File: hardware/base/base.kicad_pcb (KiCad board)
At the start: 4 copper layers, 60 x 40 mm, 70 parts, among them J1 Debug, J2 USB_B_Mini, J3 Serial Interface, J4 SWD, J5 OLED Display, J6 Conn_01x02_Pin, M1 Fan_ALT, Q1 Q_NMOS_GSD, Q2 Q_NMOS_GSD, Q3 Q_NMOS_GSD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

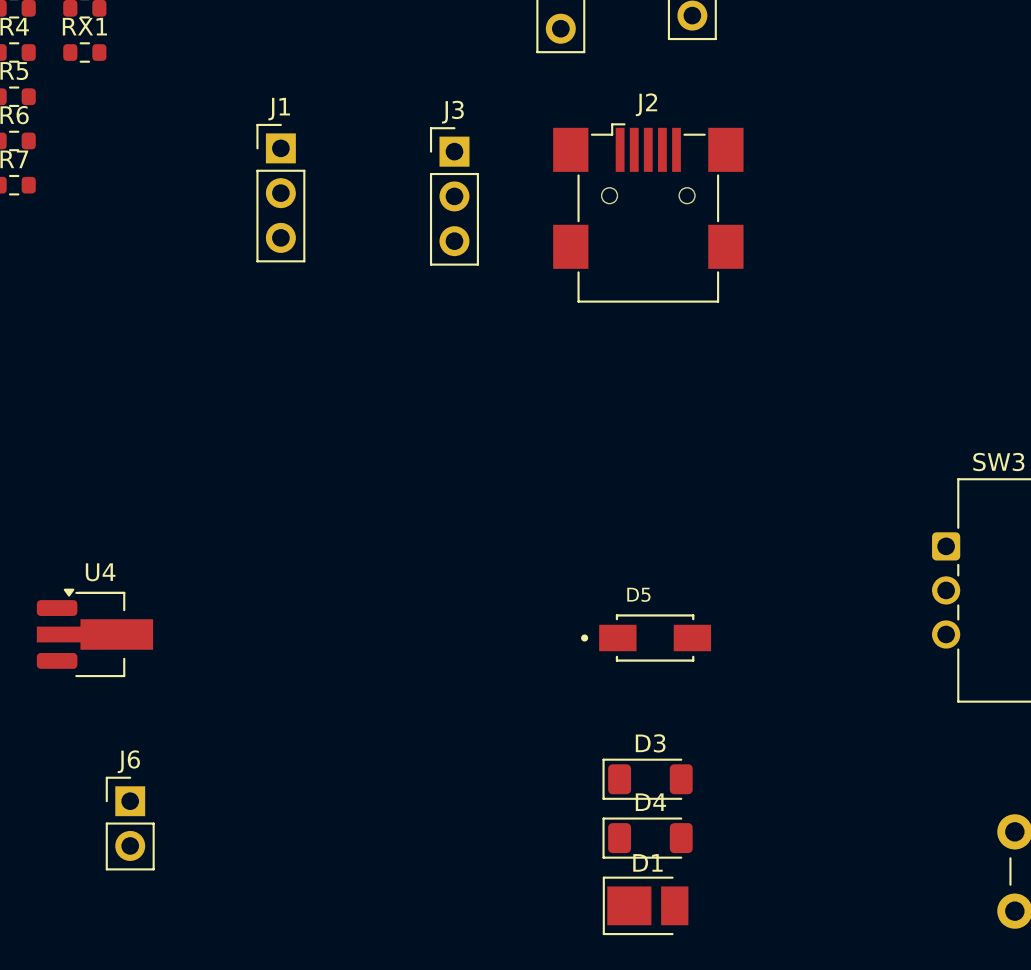
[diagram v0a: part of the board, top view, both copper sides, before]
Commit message: Update PCB and Schema after symbol change
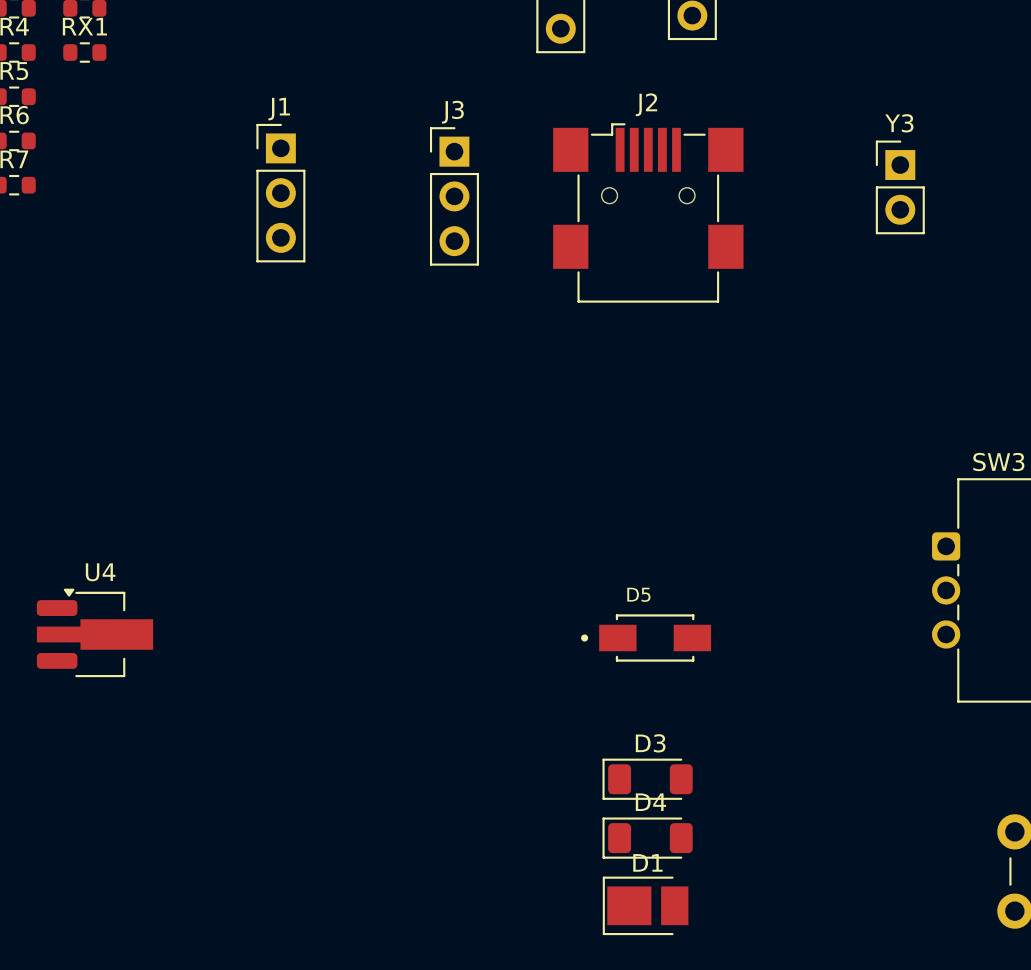
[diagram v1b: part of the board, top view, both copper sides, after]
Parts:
- removed J6: Conn_01x02_Pin, Connector_PinHeader_2.54mm:PinHeader_1x02_P2.54mm_Vertical
- added Y3: 1.70 MHz, Connector_PinHeader_2.54mm:PinHeader_1x02_P2.54mm_Vertical, F.Cu at (91.4, 60.9)

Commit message: did some layout and routing
CHANGELOG
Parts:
- moved C4 144.3 mm to (173.0, 62.7), turned to 180 degrees
- moved C3 143.8 mm to (172.7, 55.4), turned to 180 degrees
- moved C6 141.0 mm to (169.9, 62.7), turned to 180 degrees
- moved C5 140.3 mm to (169.2, 61.2)
- moved C15 138.6 mm to (170.9, 44.8)
- moved C7 136.9 mm to (166.0, 64.0), turned to 180 degrees
- moved C2 136.6 mm to (165.2, 58.4), turned to 90 degrees
- moved C8 136.1 mm to (165.2, 65.6)
- moved C21 132.0 mm to (168.6, 43.2), turned to -90 degrees
- moved C1 130.4 mm to (158.9, 56.8), turned to 90 degrees
- moved L1 129.8 mm to (170.9, 46.4), turned to 180 degrees
- moved R1 128.2 mm to (168.9, 57.1), turned to 90 degrees
- moved R4 127.5 mm to (167.9, 40.9)
- moved C9 126.8 mm to (158.1, 65.6), turned to 180 degrees
- moved R11 125.9 mm to (171.0, 48.0)
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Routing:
- net Net-(J5-Pin_4): track 0.00 -> 42.0 mm, vias 0 -> 1
- net Net-(J5-Pin_3): track 0.00 -> 41.3 mm, vias 0 -> 1
- net Net-(J4-Pin_3): track 0.00 -> 33.1 mm, vias 0 -> 2
- net Net-(J4-Pin_1): track 0.00 -> 32.3 mm, vias 0 -> 2
- net Net-(J4-Pin_2): track 0.00 -> 30.0 mm, vias 0 -> 2
- net Net-(J3-Pin_1): track 0.00 -> 26.4 mm, vias 0 -> 2
- net /VBUS: track 0.00 -> 25.7 mm, vias 0 -> 4
- net Net-(U3-OUTN): track 0.00 -> 25.4 mm
- net Net-(U3-OUTP): track 0.00 -> 24.6 mm
- net Net-(J3-Pin_2): track 0.00 -> 24.5 mm, vias 0 -> 2
- net Net-(U1-P0.01/XL2): track 0.00 -> 24.0 mm, vias 0 -> 1
- net /DETECT_VSOURCE: track 0.00 -> 24.0 mm, vias 0 -> 2
- net Net-(BT1-+): track 0.00 -> 20.9 mm, vias 0 -> 2
- net Net-(U1-P0.00/XL1): track 0.00 -> 20.4 mm, vias 0 -> 1
- net Net-(J2-D-): track 0.00 -> 20.3 mm, vias 0 -> 2
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- added copper zone on In1.Cu, net +3.3V
- added copper zone on B.Cu, net /VBUS
- added copper zone on F.Cu, net GND
- added copper zone on In2.Cu, net GND

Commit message: Changelog
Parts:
- moved SW3 3.51 mm to (117.5, 94.0)
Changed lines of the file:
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@@
 		)
 		(fp_text user "${REFERENCE}"
-			(at 0 1.270001 360)
+			(at 0 1.270001 0)
 			(layer "F.Fab")
 			(effects
@@
 		(tags "inductor")
 		(property "Reference" "L1"
-			(at 0 -1.43 360)
+			(at 0 -1.43 0)
 			(layer "F.SilkS")
 			(effects
@@
 		)
 		(property "Value" "300 uH"
-			(at 0 1.43 360)
+			(at 0 1.43 0)
 			(layer "F.Fab")
 			(effects
@@
 		)
 		(fp_text user "${REFERENCE}"
-			(at 0 0 360)
+			(at 0 0 0)
 			(layer "F.Fab")
 			(effects
@@
 		(tags "TQFN NoLead")
 		(property "Reference" "U3"
-			(at 0 -2.8 360)
+			(at 0 -2.8 0)
 			(layer "F.SilkS")
 			(effects
@@
 		)
 		(property "Value" "MAX98357A"
-			(at 0 2.8 360)
+			(at 0 2.8 0)
 			(layer "F.Fab")
 			(effects
@@
 		)
 		(fp_text user "${REFERENCE}"
-			(at 0 0 360)
+			(at 0 0 0)
 			(layer "F.Fab")
 			(effects
@@
 		(tags "capacitor")
 		(property "Reference" "C4"
-			(at 0 -1.43 360)
+			(at 0 -1.43 0)
 			(layer "F.SilkS")
 			(effects
@@
 		)
 		(property "Value" "12pF"
-			(at 0 1.43 360)
+			(at 0 1.43 0)
 			(layer "F.Fab")
 			(effects
@@
 		)
 		(fp_text user "${REFERENCE}"
-			(at 0 0 360)
+			(at 0 0 0)
 			(layer "F.Fab")
 			(effects
@@
 		(tags "capacitor")
 		(property "Reference" "C3"
-			(at 0 -1.43 360)
+			(at 0 -1.43 0)
 			(layer "F.SilkS")
 			(effects
@@
 		)
 		(property "Value" "12pF"
-			(at 0 1.43 360)
+			(at 0 1.43 0)
 			(layer "F.Fab")
 			(effects
@@
 		)
 		(fp_text user "${REFERENCE}"
-			(at 0 0 360)
+			(at 0 0 0)
 			(layer "F.Fab")
 			(effects
@@
 		(tags "QFN NoLead")
 		(property "Reference" "U1"
-			(at 0 -3.8 360)
+			(at 0 -3.8 0)
 			(layer "F.SilkS")
 			(effects
@@
 		)
 		(property "Value" "nRF52833-QDxx"
-			(at 0 3.8 360)
+			(at 0 3.8 0)
 			(layer "F.Fab")
 			(effects
@@
 		)
 		(fp_text user "${REFERENCE}"
-			(at 0 0 360)
+			(at 0 0 0)
 			(layer "F.Fab")
 			(effects
@@
 		(tags "capacitor")
 		(property "Reference" "C8"
-			(at 0 -1.43 360)
+			(at 0 -1.43 0)
 			(layer "F.SilkS")
 			(effects
@@
 		)
 		(property "Value" "100nf"
-			(at 0 1.43 360)
+			(at 0 1.43 0)
 			(layer "F.Fab")
 			(effects
@@
 		)
 		(fp_text user "${REFERENCE}"
-			(at 0 0 360)
+			(at 0 0 0)
 			(layer "F.Fab")
 			(effects
@@
 		)
 		(fp_text user "${REFERENCE}"
-			(at 0 1.270001 360)
+			(at 0 1.270001 0)
 			(layer "F.Fab")
 			(effects
@@
 		)
 		(fp_text user "${REFERENCE}"
-			(at 0 1 360)
+			(at 0 1 0)
 			(layer "F.Fab")
 			(effects
@@
 		(tags "['AT310']")
 		(property "Reference" "Y1"
-			(at -1.75 3 360)
+			(at -1.75 3 0)
 			(layer "F.SilkS")
 			(effects
@@
 		)
 		(property "Value" "32kHz"
-			(at 4.29 3 360)
+			(at 4.29 3 0)
 			(layer "F.Fab")
 			(effects
@@
 		)
 		(fp_text user "${REFERENCE}"
-			(at 1.25 8.75 360)
+			(at 1.25 8.75 0)
 			(layer "F.Fab")
 			(effects
@@
 		)
 		(fp_text user "${REFERENCE}"
-			(at 0.199999 0 360)
+			(at 0.199999 0 0)
 			(layer "F.Fab")
 			(effects
@@
 		(tags "capacitor")
 		(property "Reference" "C23"
-			(at 0 -1.43 360)
+			(at 0 -1.43 0)
 			(layer "F.SilkS")
 			(effects
@@
 		)
 		(property "Value" "0.1 uF"
-			(at 0 1.43 360)
+			(at 0 1.43 0)
 			(layer "F.Fab")
 			(effects
@@
 		)
 		(fp_text user "${REFERENCE}"
-			(at 0 0 360)
+			(at 0 0 0)
 			(layer "F.Fab")
 			(effects
@@
 		(tags "capacitor")
 		(property "Reference" "C11"
-			(at 0 -1.43 360)
+			(at 0 -1.43 0)
 			(layer "F.SilkS")
 			(effects
@@
 		)
 		(property "Value" "4.7uF"
-			(at 0 1.43 360)
+			(at 0 1.43 0)
 			(layer "F.Fab")
 			(effects
@@
 		)
 		(fp_text user "${REFERENCE}"
-			(at 0 0 360)
+			(at 0 0 0)
 			(layer "F.Fab")
 			(effects
@@
 		(tags "Through hole pin header THT 1x03 2.54mm single row")
 		(property "Reference" "J3"
-			(at 0 -2.33 360)
+			(at 0 -2.33 0)
 			(layer "F.SilkS")
 			(effects
@@
 		)
 		(property "Value" "Serial Interface"
-			(at 0 7.41 360)
+			(at 0 7.41 0)
 			(layer "F.Fab")
 			(effects
@@
 		(tags "SOT TO_SOT_SMD")
 		(property "Reference" "Q4"
-			(at 0 -2.4 360)
+			(at 0 -2.4 0)
 			(layer "F.SilkS")
 			(effects
@@
 		)
 		(property "Value" "MMBT2222A"
-			(at 0 2.4 360)
+			(at 0 2.4 0)
 			(layer "F.Fab")
 			(effects
@@
 		)
 		(fp_text user "${REFERENCE}"
-			(at 0 0 360)
+			(at 0 0 0)
 			(layer "F.Fab")
 			(effects
@@
 	(footprint "Rotary_Encoder:RotaryEncoder_Bourns_Vertical_PEC12R-3x17F-Sxxxx"
 		(layer "F.Cu")
-		(at 117.75 97.5)
+		(at 117.5 94)
 		(descr "Bourns rotary encoder, PEC12R, with switch, with bushing, vertical shaft, 17.5mm shaft, https://www.bourns.com/docs/product-datasheets/pec12r.pdf")
 		(tags "rotary encoder")
@@
 		(tags "test point THT pad rectangle square")
 		(property "Reference" "TP1"
-			(at 0 -1.648 360)
+			(at 0 -1.648 0)
 			(layer "F.SilkS")
 			(effects
@@
 		)
 		(property "Value" "TestPoint"
-			(at 0 1.75 360)
+			(at 0 1.75 0)
 			(layer "F.Fab")
 			(effects
@@
 		)
 		(fp_text user "${REFERENCE}"
-			(at 0 -1.65 360)
+			(at 0 -1.65 0)
 			(layer "F.Fab")
 			(effects
@@
 		(tags "SOT TO_SOT_SMD")
 		(property "Reference" "Q2"
-			(at 0 -2.4 360)
+			(at 0 -2.4 0)
 			(layer "F.SilkS")
 			(effects
@@
 		)
 		(property "Value" "Q_NMOS_GSD"
-			(at 0 2.4 360)
+			(at 0 2.4 0)
 			(layer "F.Fab")
 			(effects
@@
 		)
 		(fp_text user "${REFERENCE}"
-			(at 0 0 360)
+			(at 0 0 0)
 			(layer "F.Fab")
 			(effects
@@
 		(tags "capacitor")
 		(property "Reference" "C16"
-			(at 0 -1.43 360)
+			(at 0 -1.43 0)
 			(layer "F.SilkS")
 			(effects
@@
 		)
 		(property "Value" "1uF"
-			(at 0 1.43 360)
+			(at 0 1.43 0)
 			(layer "F.Fab")
 			(effects
@@
 		)
 		(fp_text user "${REFERENCE}"
-			(at 0 0 360)
+			(at 0 0 0)
 			(layer "F.Fab")
 			(effects
@@
 		(tags "capacitor")
 		(property "Reference" "C10"
-			(at 0 -1.43 360)
+			(at 0 -1.43 0)
 			(layer "F.SilkS")
 			(effects
@@
 		)
 		(property "Value" "4.7uF"
-			(at 0 1.43 360)
+			(at 0 1.43 0)
 			(layer "F.Fab")
 			(effects
@@
 		)
 		(fp_text user "${REFERENCE}"
-			(at 0 0 360)
+			(at 0 0 0)
 			(layer "F.Fab")
 			(effects
@@
 		(tags "Through hole pin header THT 1x04 2.54mm single row")
 		(property "Reference" "J5"
-			(at 0 -2.33 360)
+			(at 0 -2.33 0)
 			(layer "F.SilkS")
 			(effects
@@
 		)
 		(property "Value" "OLED Display"
-			(at 0.2 11.6 360)
+			(at 0.2 11.6 0)
 			(layer "F.Fab")
 			(effects
@@
 		(tags "capacitor")
 		(property "Reference" "C6"
-			(at 0 -1.43 360)
+			(at 0 -1.43 0)
 			(layer "F.SilkS")
 			(effects
@@
 		)
 		(property "Value" "1uF"
-			(at 0 1.43 360)
+			(at 0 1.43 0)
 			(layer "F.Fab")
 			(effects
@@
 		)
 		(fp_text user "${REFERENCE}"
-			(at 0 0 360)
+			(at 0 0 0)
 			(layer "F.Fab")
 			(effects
@@
 		(tags "resistor")
 		(property "Reference" "R6"
-			(at 0 -1.43 360)
+			(at 0 -1.43 0)
 			(layer "F.SilkS")
 			(effects
@@
 		)
 		(property "Value" "10k"
-			(at 0 1.43 360)
+			(at 0 1.43 0)
 			(layer "F.Fab")
 			(effects
@@
 		)
 		(fp_text user "${REFERENCE}"
-			(at 0 0 360)
+			(at 0 0 0)
 			(layer "F.Fab")
 			(effects
@@
 		(tags "capacitor")
 		(property "Reference" "C7"
-			(at 0 -1.43 360)
+			(at 0 -1.43 0)
 			(layer "F.SilkS")
 			(effects
@@
 		)
 		(property "Value" "820pF"
-			(at 0 1.43 360)
+			(at 0 1.43 0)
 			(layer "F.Fab")
 			(effects
@@
 		)
 		(fp_text user "${REFERENCE}"
-			(at 0 0 360)
+			(at 0 0 0)
 			(layer "F.Fab")
 			(effects
@@
 		(tags "capacitor")
 		(property "Reference" "C9"
-			(at 0 -1.43 360)
+			(at 0 -1.43 0)
 			(layer "F.SilkS")
 			(effects
@@
 		)
 		(property "Value" "4.7uf"
-			(at 0 1.43 360)
+			(at 0 1.43 0)
 			(layer "F.Fab")
 			(effects
@@
 		)
 		(fp_text user "${REFERENCE}"
-			(at 0 0 360)
+			(at 0 0 0)
 			(layer "F.Fab")
 			(effects
@@
 		(tags "capacitor")
 		(property "Reference" "C5"
-			(at 0 -1.43 360)
+			(at 0 -1.43 0)
 			(layer "F.SilkS")
 			(effects
@@
 		)
 		(property "Value" "100pF"
-			(at 0 1.43 360)
+			(at 0 1.43 0)
 			(layer "F.Fab")
 			(effects
@@
 		)
 		(fp_text user "${REFERENCE}"
-			(at 0 0 360)
+			(at 0 0 0)
 			(layer "F.Fab")
 			(effects

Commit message: finished placing components
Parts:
- removed C21: 100 nF, Capacitor_SMD:C_0603_1608Metric
- removed D5: SS16, Schottky Rectifier (SS16):DIOM4325X250N
- removed L1: 300 uH, Inductor_SMD:L_0603_1608Metric
- removed Q4: MMBT2222A, Package_TO_SOT_SMD:SOT-23
- removed RX1: 664k, Resistor_SMD:R_0603_1608Metric
- added D2: D_Schottky, Schottky Diode (ZLLS500TA):SOT91P240X110-3N, F.Cu at (130.4, 61.0)
- BT1: moved to B.Cu
- C15: value 100 nF -> 10nF
- D3, D4: footprint Diode_SMD:D_MiniMELF -> Schottky Diode (ZLLS500TA):SOT91P240X110-3N
- R10: value 10kOhm -> 150 kOhm
- R11: value 100 Ohm -> 470 kOhm
- R5: value 100 Ohm -> 10k
- R7: value 100 Ohm -> 22 Ohm
- R9: value 132 kOhm -> 100 kOhm
- moved C17 78.4 mm to (141.5, 26.0), turned to -90 degrees
- moved SW3 73.5 mm to (144.2, 25.5)
- moved C18 71.1 mm to (141.5, 30.0)
- moved LS1 68.4 mm to (178.0, 28.3), turned to 180 degrees
- moved GND3 57.0 mm to (179.0, 21.0)
- moved J1 55.2 mm to (178.0, 56.5), turned to -90 degrees
- moved J3 52.0 mm to (128.4, 77.8)
- moved J4 50.9 mm to (133.8, 70.2)
- moved U3 50.4 mm to (173.5, 23.0), turned to 0 degrees
- moved C19 41.0 mm to (172.0, 28.5), turned to 90 degrees
- moved C20 40.7 mm to (174.4, 28.5), turned to 90 degrees
- moved C12 38.7 mm to (143.5, 39.3), turned to 90 degrees
- moved GND4 36.8 mm to (179.0, 78.4)
- moved B1 36.2 mm to (159.5, 77.7), turned to 180 degrees
- moved R1 36.0 mm to (163.0, 21.5)
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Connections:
- B1 pad 1: (no net) -> Net-(B1-Pad1)
- B1 pad 2: (no net) -> Net-(D3-A)
- C15 pad 1: Net-(Q3-D) -> /ROT_ENC_S1
- C15 pad 2: Net-(C15-Pad2) -> GND
- C16 pad 1: Net-(J5-Pin_2) -> +3.3V
- C23 pad 1: +3.3V -> /VBUS
- C23 pad 2: Net-(D5-A) -> Net-(D3-A)
- D3 pad 1: +3.3V -> /VBUS
- D3 pad 2: Net-(BT1-+) -> Net-(D3-A)
- J5 pad 2: Net-(J5-Pin_2) -> +3.3V
- Q1 pad 1: Net-(Q1-G) -> /LED
- Q2 pad 1: Net-(Q2-G) -> /AMP_FAN_HUM
- Q3 pad 1: /HUMIDIFIER_MOSFET_GATE -> /HAPTIC
- Q3 pad 2: Net-(Q3-S) -> GND
- Q3 pad 3: Net-(Q3-D) -> Net-(D3-A)
- R10 pad 1: /HUMIDIFIER_MOSFET_GATE -> /AMP_FAN_HUM
- R10 pad 2: GND -> Net-(R10-Pad2)
- R11 pad 1: Net-(Q3-S) -> Net-(R10-Pad2)
- R11 pad 2: GND -> Net-(U3-~{SD_MODE})
- R2 pad 1: Net-(Q1-G) -> /LED
- R5 pad 1: /HUMIDIFIER_MOSFET_GATE -> /HAPTIC
- R5 pad 2: /HUMIDIFIER_MOSFET_GATE -> GND
- R6 pad 1: Net-(Q2-G) -> /AMP_FAN_HUM
- R7 pad 1: /LED_HAPTIC -> /VBUS
- R7 pad 2: Net-(Q1-G) -> Net-(B1-Pad1)
- TP1 pad 1: /LED_HAPTIC -> /LED
- TP2 pad 1: Net-(Q2-G) -> /AMP_FAN_HUM
- TP4 pad 1: /HUMIDIFIER_MOSFET_GATE -> /AMP_DIN
- U1 pad 17: /HUMIDIFIER_MOSFET_GATE -> /HAPTIC
- U1 pad 22: /DETECT_VSOURCE -> /LED
- U1 pad 23: Net-(Q2-G) -> /AMP_FAN_HUM
- U1 pad 32: /LED_HAPTIC -> /DETECT_VSOURCE
- U3 pad 17: unconnected-(U3-PAD-Pad17) -> GND
- Y3 pad 1: GND -> /VBUS
- Y3 pad 2: Net-(C15-Pad2) -> Net-(M1-+)
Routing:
- net Net-(J5-Pin_4): track 42.0 -> 0.00 mm, vias 1 -> 0
- net Net-(J5-Pin_3): track 41.3 -> 0.00 mm, vias 1 -> 0
- net Net-(J4-Pin_3): track 33.1 -> 0.00 mm, vias 2 -> 0
- net Net-(J4-Pin_1): track 32.3 -> 0.00 mm, vias 2 -> 0
- net Net-(J4-Pin_2): track 30.0 -> 0.00 mm, vias 2 -> 0
- net Net-(J3-Pin_1): track 26.4 -> 0.00 mm, vias 2 -> 0
- net /VBUS: track 25.7 -> 0.00 mm, vias 4 -> 0
- net Net-(U3-OUTN): track 25.4 -> 0.00 mm
- net Net-(U3-OUTP): track 24.6 -> 0.00 mm
- net Net-(J3-Pin_2): track 24.5 -> 0.00 mm, vias 2 -> 0
- net Net-(U1-P0.01/XL2): track 24.0 -> 0.00 mm, vias 1 -> 0
- net /DETECT_VSOURCE: track 24.0 -> 0.00 mm, vias 2 -> 0
- net Net-(BT1-+): track 20.9 -> 0.00 mm, vias 2 -> 0
- net Net-(U1-P0.00/XL1): track 20.4 -> 0.00 mm, vias 1 -> 0
- net Net-(J2-D-): track 20.3 -> 0.00 mm, vias 2 -> 0
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- added copper zone on B.Cu, net GND
- added copper zone on In1.Cu, net GND
- removed copper zone on In1.Cu, net +3.3V
- removed copper zone on B.Cu, net /VBUS
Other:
- board size 60 x 40 mm -> 60 x 60 mm

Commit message: fix references
Co-authored-by: yuvve <yuvve@users.noreply.github.com>
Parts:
- moved R2 2.38 mm to (169.5, 42.5)
- moved D1 2.31 mm to (174.0, 36.5)
- moved Q1 2.31 mm to (173.1, 42.1)
- moved R3 2.31 mm to (176.5, 40.7)
- moved R4 2.31 mm to (176.5, 44.3)
- moved TP1 2.31 mm to (169.5, 39.0)
- moved Q3 2.00 mm to (154.7, 70.9)
- moved Q2 1.51 mm to (163.5, 70.5)
- moved TP2 1.51 mm to (163.0, 66.6)
- moved U3 1.04 mm to (173.5, 24.0)
- moved C23 1.00 mm to (150.5, 73.0)
- moved R10 1.00 mm to (169.0, 28.5)
- moved R5 1.00 mm to (154.6, 75.5)
- moved R9 1.00 mm to (163.2, 51.5)
- moved R8 0.95 mm to (167.4, 51.5)
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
